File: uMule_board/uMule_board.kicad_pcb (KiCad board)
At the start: 2 copper layers, 140 x 140 mm, 148 parts, among them J1 12V IN, J10 Conn_01x04, J11 Conn_01x04, J12 Conn_01x04, J13 Conn_01x04, J14 Conn_01x04, J2 Dynamixel, J3 Li-Dar_UART, J4 ESP32_UART, J5 Conn_ST_STDC14, J6 I2C, J7 SPI_IMU, J8 Conn_02x04_Odd_Even, J9 Conn_02x04_Odd_Even, P1 BPV10NF, P2 BPV10NF, P3 BPV10NF, P4 BPV10NF, P5 BPV10NF, P6 BPV10NF, P7 BPV10NF, P8 BPV10NF, Q1 AON6407, Q2 S9015, SW1 DBG_BUTT, SW2 RST, U1 TPS62933, U10 OPA397DBVR, U11 OPA397DBVR, U12 OPA397DBVR, U13 OPA397DBVR, U14 OPA397DBVR, U15 OPA397DBVR, U16 SP3485CN, U2 TLV761, U3 LM431BMC3, U4 INA219AxD, U5 TPS62933, U6 STM32F103RCTx, U7 FM24C64B, U8 OPA397DBVR, U9 OPA397DBVR, Y1 8MHz

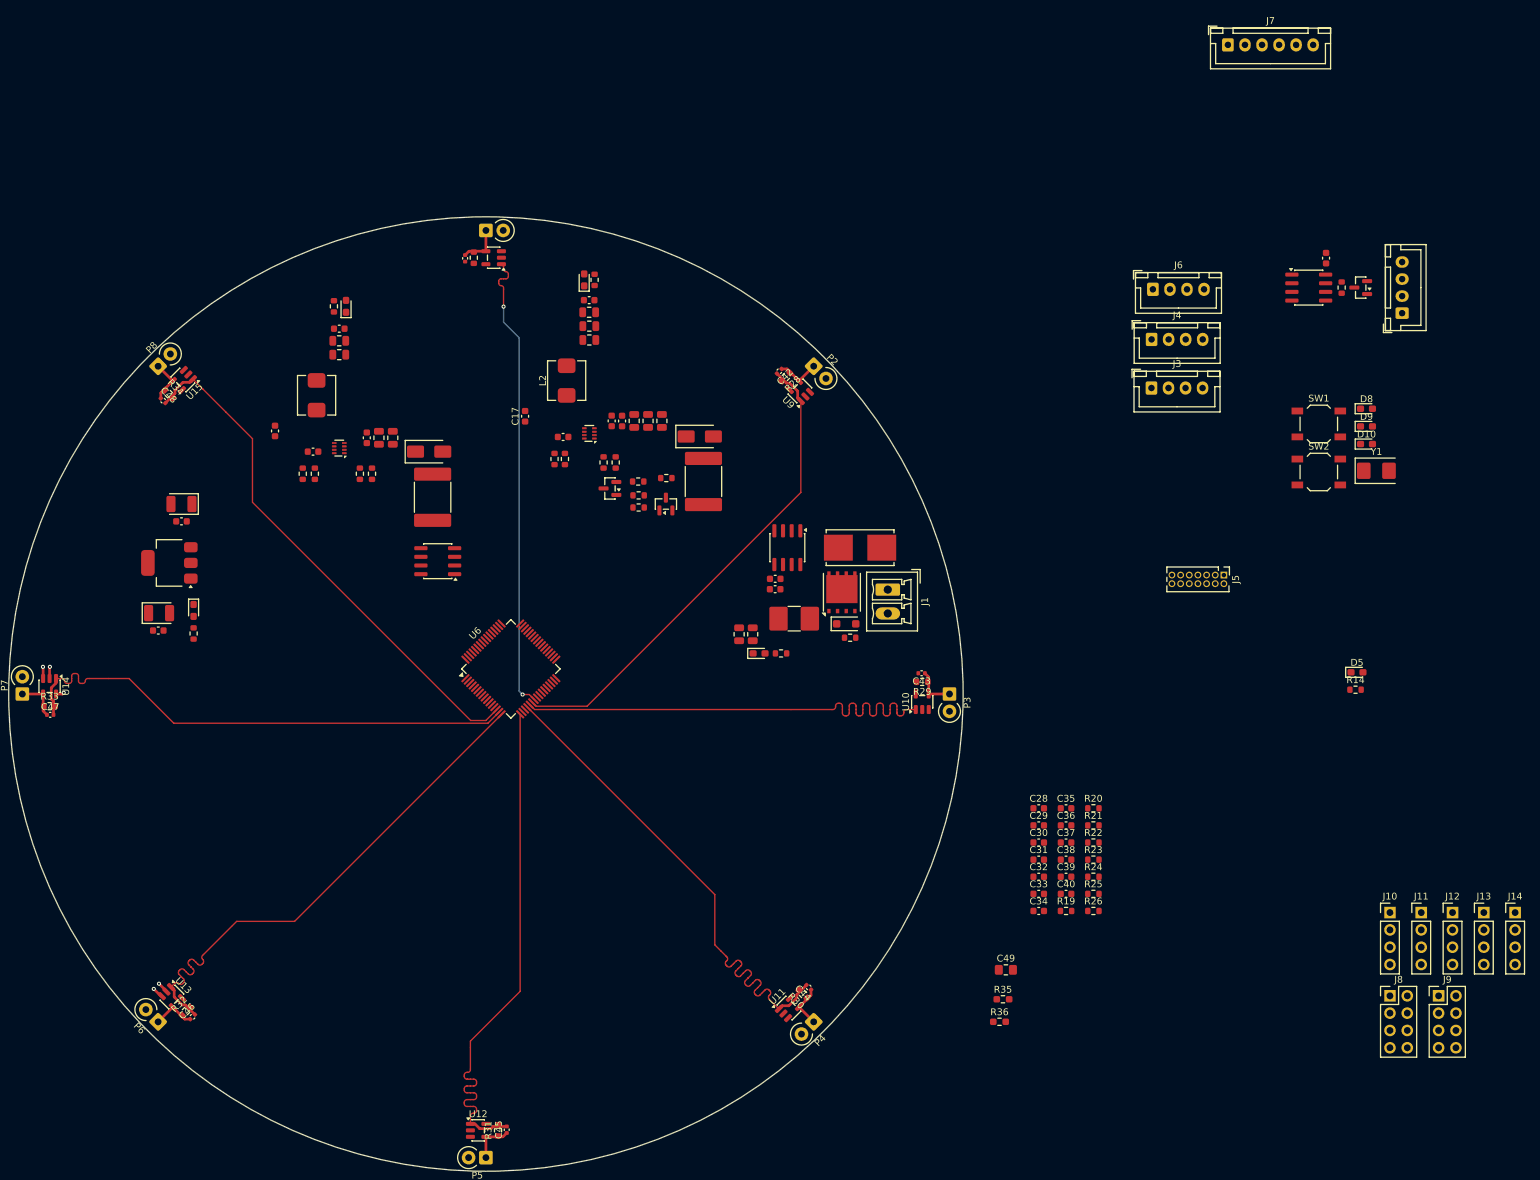
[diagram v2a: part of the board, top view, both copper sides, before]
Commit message: another day, more progress. Elements are placed on board, traces need to be conected, added jumpers for power in case of bad design
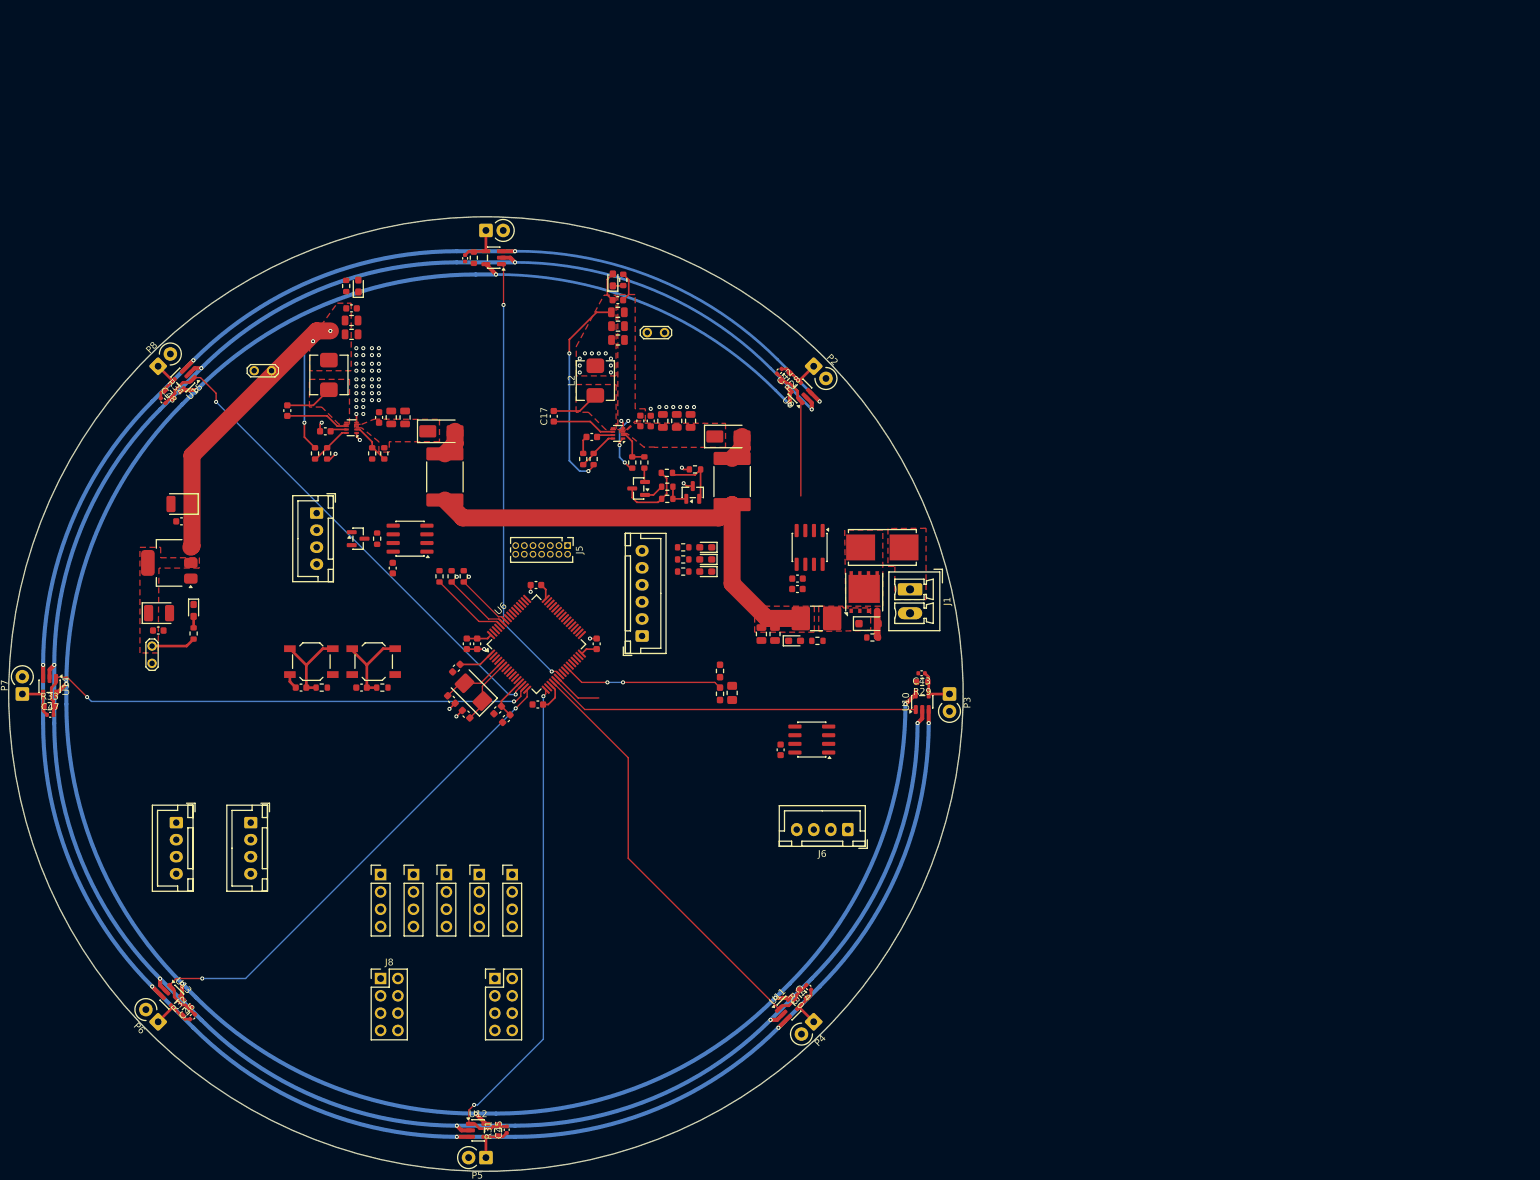
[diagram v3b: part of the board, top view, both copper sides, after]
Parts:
- removed the D5 at (168.0, 109.3)
- removed the D5 at (255.7, 112.1)
- removed the R14 at (171.3, 109.3)
- removed the R14 at (255.5, 114.6)
- added D5: LED, LED_SMD:LED_0603_1608Metric_Pad1.05x0.95mm_HandSolder, F.Cu at (173.2, 107.4)
- added JP1: Jumper_2_Open, TestPoint:TestPoint_2Pads_Pitch2.54mm_Drill0.8mm, F.Cu at (96.5, 67.8)
- added JP2: Jumper_2_Open, TestPoint:TestPoint_2Pads_Pitch2.54mm_Drill0.8mm, F.Cu at (79.0, 108.2)
- added JP3: Jumper_2_Open, TestPoint:TestPoint_2Pads_Pitch2.54mm_Drill0.8mm, F.Cu at (151.6, 62.2)
- added R14: 14k, Resistor_SMD:R_0603_1608Metric, F.Cu at (176.6, 107.4)
- moved J2 161.9 mm to (103.1, 88.7), turned to -90 degrees
- moved J3 156.6 mm to (82.5, 134.1), turned to -90 degrees
- moved J12 152.5 mm to (117.3, 141.7)
- moved J13 152.3 mm to (122.2, 141.7)
- moved J14 152.0 mm to (127.0, 141.7)
- moved SW1 151.8 mm to (102.4, 110.5)
- moved D11 151.6 mm to (109.2, 92.5), turned to 0 degrees
- moved J4 150.0 mm to (93.5, 134.1), turned to -90 degrees
- moved J10 148.2 mm to (112.5, 141.7)
- moved J8 148.1 mm to (112.5, 157.0)
- moved R37 146.2 mm to (112.0, 92.5), turned to 90 degrees
- moved C50 144.3 mm to (114.3, 96.8), turned to 90 degrees
- moved SW2 141.4 mm to (111.5, 110.5)
- moved J9 138.5 mm to (129.3, 157.0)
- moved U16 136.9 mm to (116.8, 92.5), turned to 180 degrees
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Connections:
- C11 pad 1: +5V -> /Power/+5V
- C12 pad 1: +5V -> /Power/+5V
- C13 pad 1: +3V3 -> /Power/+3V3
- C14 pad 1: +3V3 -> /Power/+3V3
- C15 pad 1: +3V3 -> /Power/+3V3
- C16 pad 1: +3V3 -> /Power/+3V3
- C22 pad 2: -5V -> /Power/-5V
- C23 pad 2: -5V -> /Power/-5V
- C24 pad 2: -5V -> /Power/-5V
- C25 pad 2: -5V -> /Power/-5V
- C26 pad 2: -5V -> /Power/-5V
- C27 pad 2: -5V -> /Power/-5V
- C5 pad 1: +5V -> /Power/+5V
- C6 pad 1: +5V -> /Power/+5V
- C7 pad 1: +5V -> /Power/+5V
- L1 pad 2: +5V -> /Power/+5V
- R11 pad 2: -5V -> /Power/-5V
- R13 pad 1: -5V -> /Power/-5V
- R15 pad 1: +5V -> /Power/+5V
- R16 pad 1: +3V3 -> /Power/+3V3
- R18 pad 2: -5V -> /Power/-5V
- R3 pad 1: +5V -> /Power/+5V
- U2 pad 2: +3V3 -> /Power/+3V3
- U2 pad 3: +5V -> /Power/+5V
- U4 pad 5: +3V3 -> /Power/+3V3
- U5 pad 1: -5V -> /Power/-5V
- U5 pad 4: -5V -> /Power/-5V
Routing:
- net /Photodiodes/V_{REF}: track 3.35 -> 397.8 mm, vias 2 -> 10
- net -5V: track 3.34 -> 367.6 mm, vias 2 -> 8
- net +5V: track 1.20 -> 354.4 mm, vias 1 -> 8
- net VCC: track 0.00 -> 67.8 mm
- net /Power/+5V: track 0.00 -> 58.2 mm, vias 0 -> 3
- net GND: track 0.00 -> 52.1 mm, vias 0 -> 65
- net /Photodiodes/PHO_1: track 71.8 -> 26.9 mm
- net +3V3: track 0.00 -> 24.4 mm
- net /Power/-5V: track 0.00 -> 17.8 mm, vias 0 -> 4
- net /Photodiodes/PHO_2: track 71.1 -> 54.7 mm
- net /MCU/NRST: track 0.00 -> 13.2 mm
- net /MCU/DBG_BTN: track 0.00 -> 13.0 mm
- net /MCU/BOOT: track 0.00 -> 11.6 mm
- net /MCU/I2C1_SDA: track 0.00 -> 11.1 mm, vias 0 -> 1
- net /Power/INV_CONV_IN: track 0.00 -> 10.6 mm
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- added copper zone on F.Cu, net /Power/+3V3
- added copper zone on F.Cu, net /Power/+5V
- added copper zone on F.Cu, net /Power/-5V
- added copper zone on F.Cu, net /Power/DC_CONV_IN
- added copper zone on F.Cu, net /Power/INV_CONV_IN
- added copper zone on F.Cu, net /Power/R_SHUNT_+
- added copper zone on F.Cu, net /Power/VSUP+
- added copper zone on F.Cu, net GND
- added copper zone on F.Cu, net Net-(Q1-D)
- added copper zone on F.Cu, net Net-(U1-SW)
- added copper zone on F.Cu, net Net-(U5-SW)
- added copper zone on F.Cu, net VCC

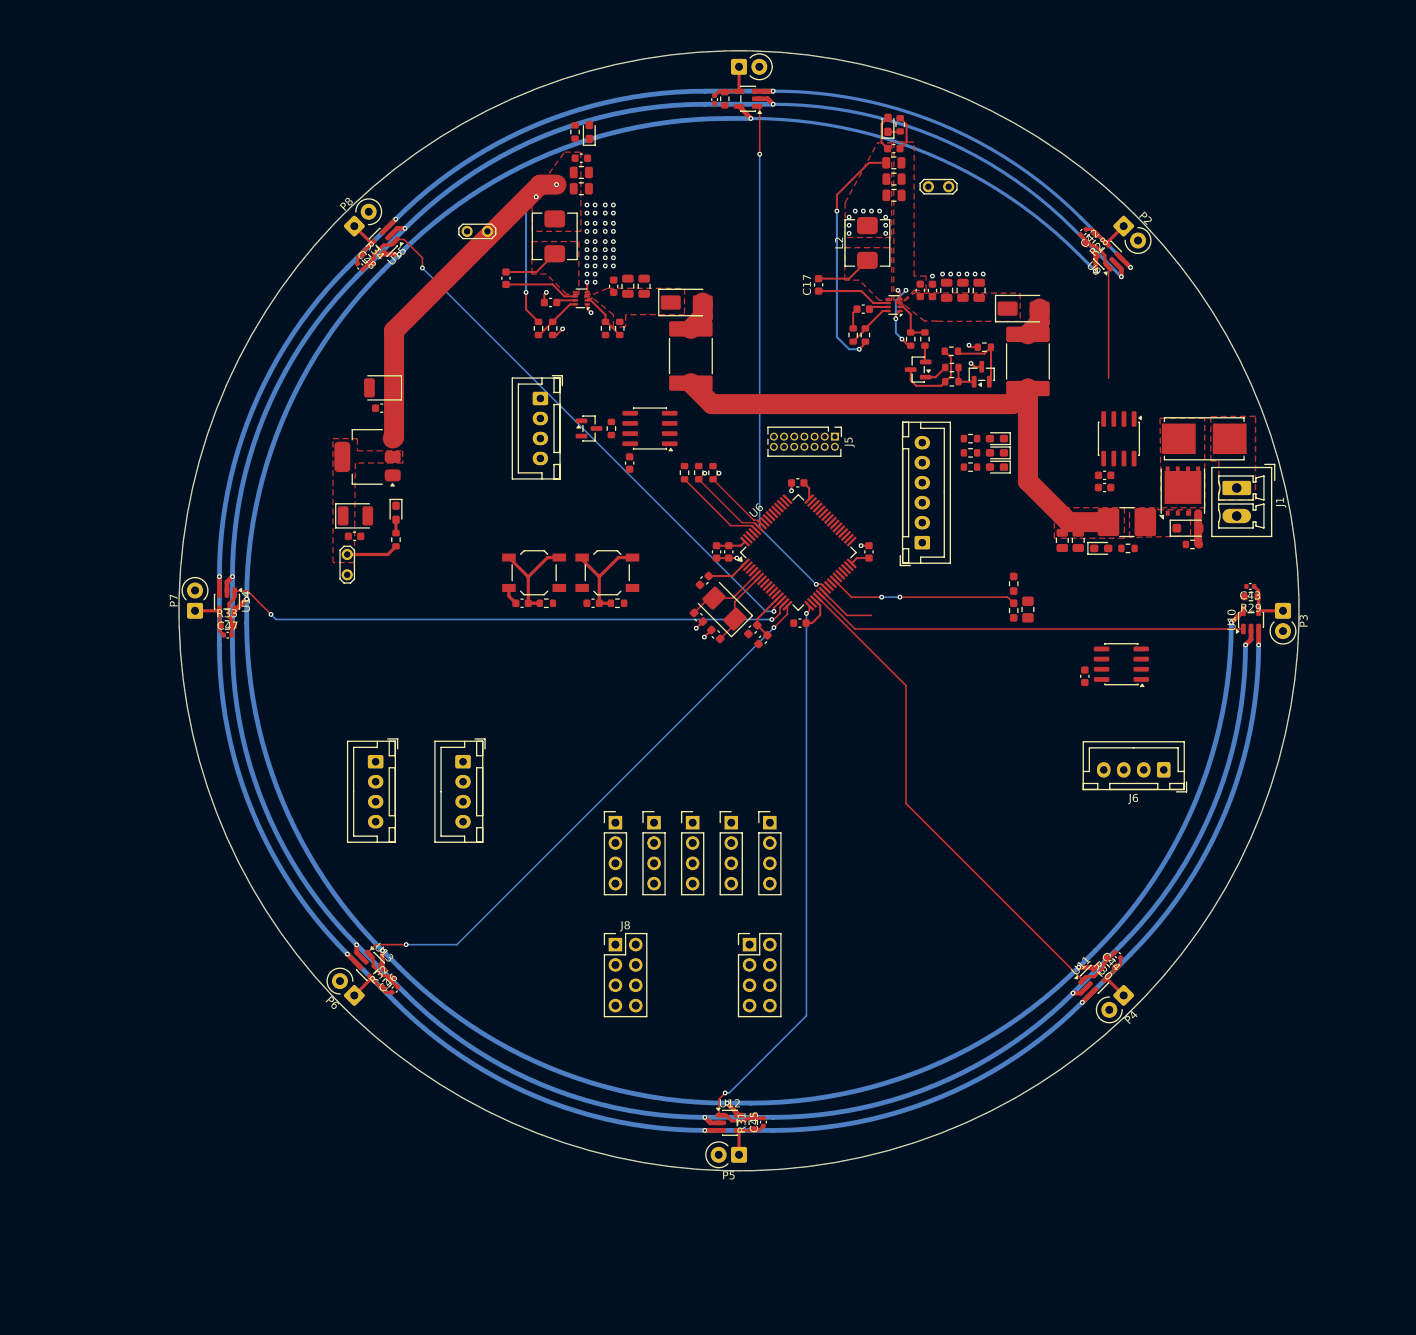
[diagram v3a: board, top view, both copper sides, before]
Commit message: DRC Passed, now only slight modifications on traces left, lenght matching and proper board description
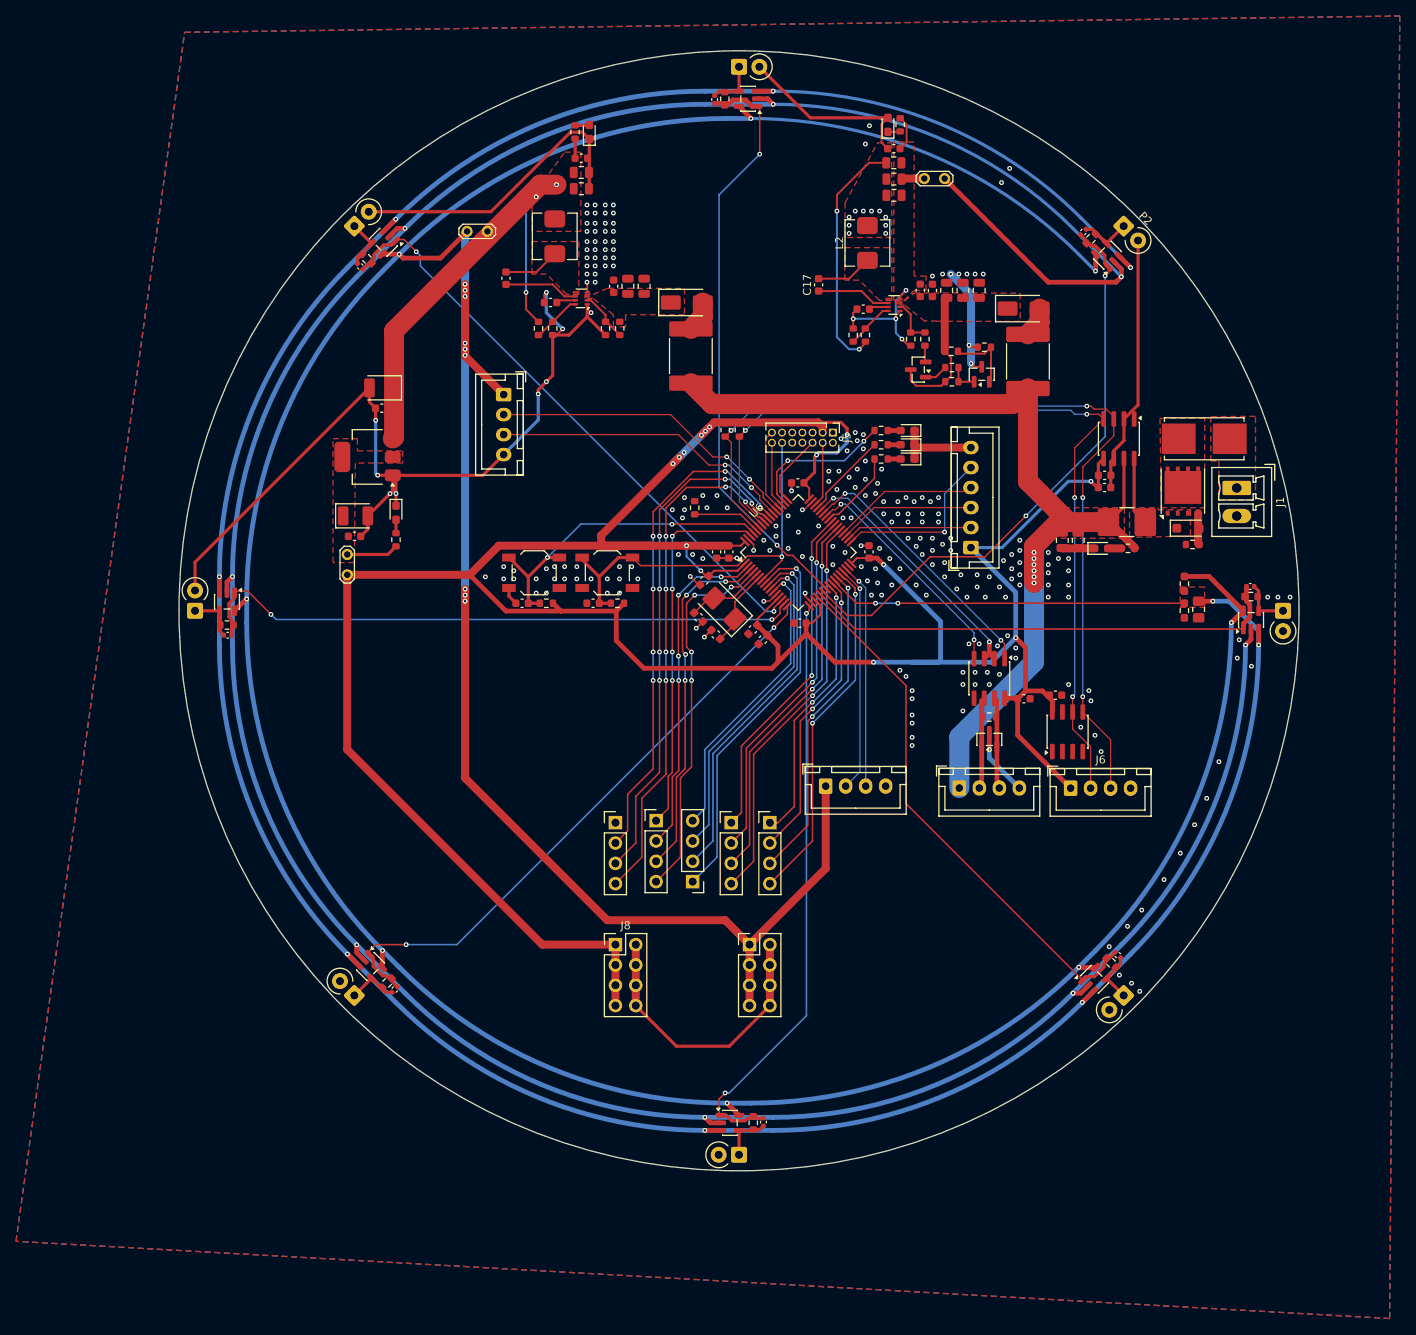
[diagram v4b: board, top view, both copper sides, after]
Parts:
- moved J2 71.5 mm to (155.5, 137.4), turned to 0 degrees
- moved D11 63.4 mm to (159.3, 131.3), turned to 90 degrees
- moved R37 59.4 mm to (159.3, 128.5), turned to 180 degrees
- moved C50 57.4 mm to (163.6, 126.2), turned to 180 degrees
- moved J3 56.3 mm to (138.8, 137.2), turned to 0 degrees
- moved U16 52.7 mm to (159.3, 123.7), turned to -90 degrees
- moved J4 46.2 mm to (98.6, 88.2)
- moved C49 21.3 mm to (185.4, 115.1)
- moved R35 21.3 mm to (183.6, 111.9)
- moved R36 21.3 mm to (183.6, 115.2)
- moved J11 14.2 mm to (117.6, 141.5)
- moved J6 11.9 mm to (169.4, 137.4), turned to 0 degrees
- moved D8 11.2 mm to (149.0, 92.7)
- moved D9 11.2 mm to (149.0, 94.5)
- moved D10 11.2 mm to (149.0, 96.3)
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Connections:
- C13 pad 1: /Power/+3V3 -> /Power/+3V3_POW
- C14 pad 1: /Power/+3V3 -> /Power/+3V3_POW
- C15 pad 1: /Power/+3V3 -> +3V3
- C16 pad 1: /Power/+3V3 -> +3V3
- J10 pad 2: /GPIO/GPIO_1 -> /GPIO/GPIO_3
- J10 pad 3: /GPIO/GPIO_2 -> /GPIO/GPIO_4
- J10 pad 4: /GPIO/GPIO_3 -> /GPIO/GPIO_5
- J11 pad 1: /GPIO/GPIO_4 -> /GPIO/GPIO_6
- J11 pad 2: /GPIO/GPIO_5 -> /GPIO/GPIO_18
- J11 pad 3: /GPIO/GPIO_6 -> /GPIO/GPIO_19
- J13 pad 3: /GPIO/GPIO_14 -> /GPIO/GPIO_1
- J13 pad 4: /GPIO/GPIO_15 -> /GPIO/GPIO_2
- J14 pad 1: /GPIO/GPIO_16 -> /GPIO/GPIO_17
- J14 pad 2: /GPIO/GPIO_17 -> /GPIO/GPIO_16
- J14 pad 3: /GPIO/GPIO_18 -> /GPIO/GPIO_15
- J14 pad 4: /GPIO/GPIO_19 -> /GPIO/GPIO_14
- JP2 pad 1: /Power/+3V3 -> /Power/+3V3_POW
- R16 pad 1: /Power/+3V3 -> /Power/+3V3_POW
- U2 pad 2: /Power/+3V3 -> /Power/+3V3_POW
- U4 pad 5: /Power/+3V3 -> +3V3
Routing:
- net +3V3: track 24.4 -> 387.4 mm, vias 0 -> 14
- net GND: track 52.1 -> 330.4 mm, vias 65 -> 261
- net +5V: track 354.4 -> 531.2 mm, vias 8 -> 17
- net /MCU/I2C1_SDA: track 11.1 -> 113.3 mm, vias 1 -> 4
- net /MCU/I2C1_SCL: track 9.55 -> 108.2 mm, vias 1 -> 4
- net /GPIO/GPIO_5: track 0.00 -> 65.1 mm, vias 0 -> 6
- net /GPIO/GPIO_4: track 0.00 -> 63.9 mm, vias 0 -> 6
- net /GPIO/GPIO_3: track 0.00 -> 62.7 mm, vias 0 -> 6
- net VCC: track 67.8 -> 127.8 mm, vias 0 -> 6
- net /GPIO/GPIO_14: track 0.00 -> 49.9 mm, vias 0 -> 2
- net /GPIO/GPIO_8: track 0.00 -> 49.6 mm, vias 0 -> 1
- net /GPIO/GPIO_15: track 0.00 -> 47.5 mm, vias 0 -> 2
- net /GPIO/GPIO_7: track 0.00 -> 46.9 mm, vias 0 -> 4
- net /GPIO/GPIO_6: track 0.00 -> 46.7 mm, vias 0 -> 4
- net /Photodiodes/PHO_1: track 26.9 -> 72.8 mm, vias 0 -> 2
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- added copper zone on F.Cu, net /Photodiodes/V_{REF}
- added copper zone on F.Cu, net /Power/+3V3_POW
- added copper zone on B.Cu, net GND
- removed copper zone on F.Cu, net /Power/+3V3
